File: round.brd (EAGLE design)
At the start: 50 x 50 mm, 8 parts, among them IC1 MC9S08GT8A-48, U1 USD-SOCKETNEW, U2 MCP73831, U3 ADXL345, U5 RFM69CW

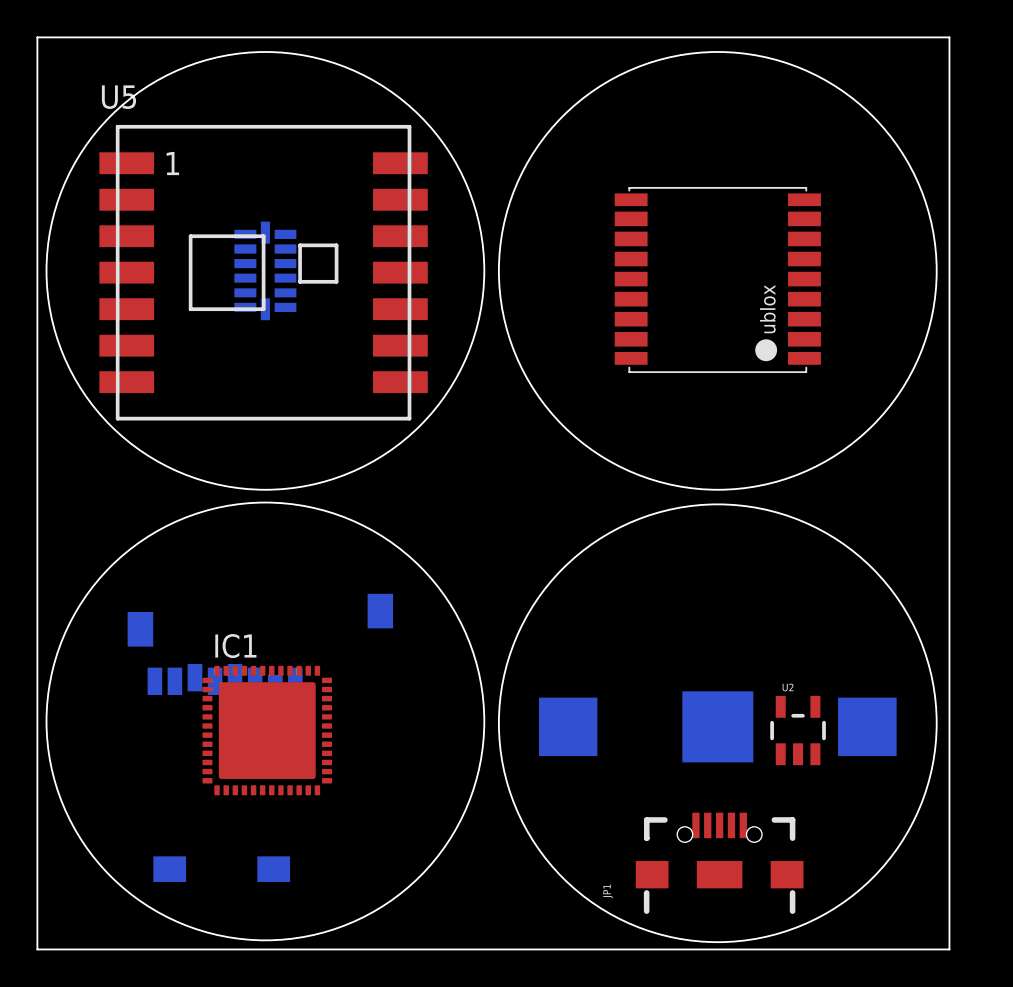
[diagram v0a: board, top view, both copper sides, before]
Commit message: Added power supply to round boards.
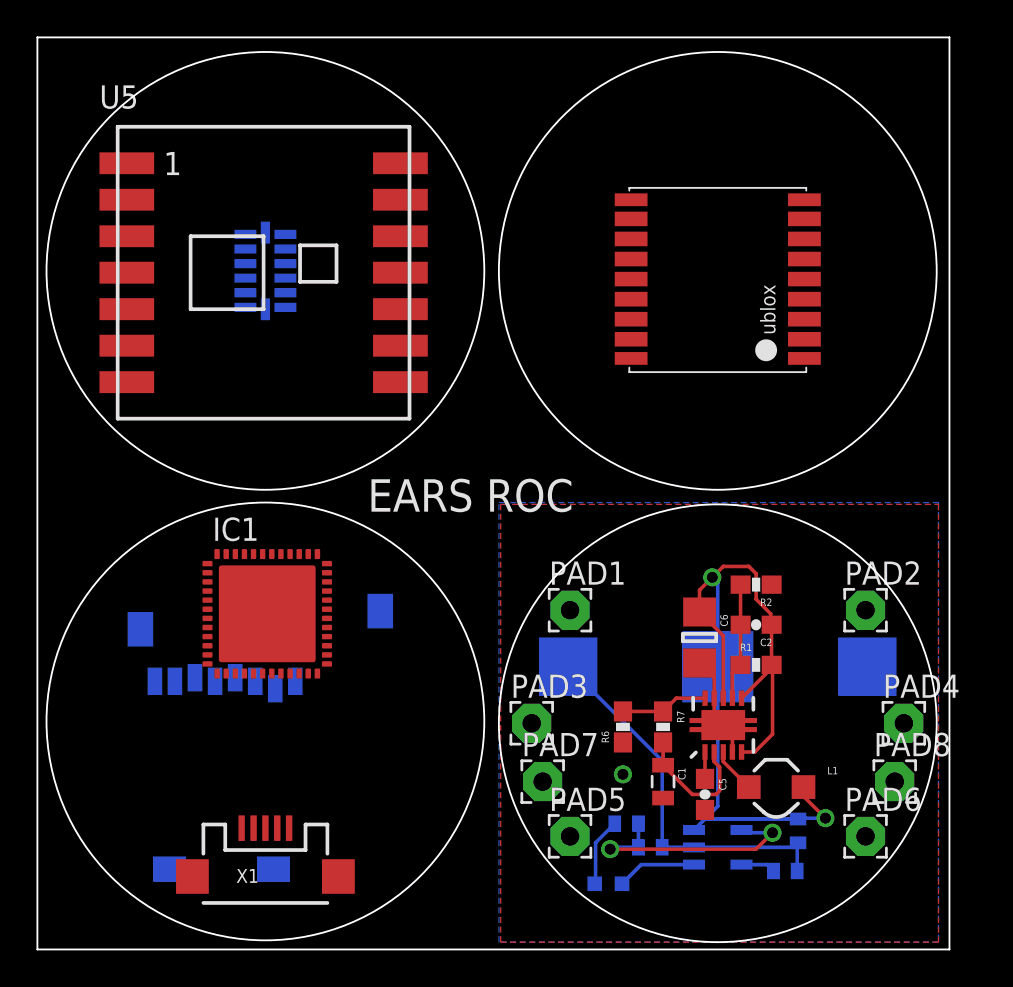
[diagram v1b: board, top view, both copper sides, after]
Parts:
- removed JP1: USB_MICROB_PLUGCONN-11752, SparkFun-Connectors:USB-B-MICRO-SMD_V03
- removed U2: MCP73831, SparkFun-PowerIC:SOT23-5
- added C1: 22uF, CH_passive:0805
- added C2, C5: 0.1uF, SparkFun:0603-CAP
- added C3, C4: 4.7uF, SparkFun:0402-CAP
- added C6: 10uF, CH_passive:1206
- added D11: RED, SparkFun:LED-0603
- added L1: 4.7uH, 1.2A, SparkFun:CDRH2D09
- added PAD1, PAD2, PAD3, PAD4, PAD5, PAD6, PAD7, PAD8: (no value), wirepad:2,15/1,0
- added R1, R7: 2M, SparkFun:0603-RES
- added R2, R6: 220k, SparkFun:0603-RES
- added R3: 330, SparkFun:0402-RES
- added R4: 2K, SparkFun:0402-RES
- added U4: MCP73831, SparkFun:SOT23-5
- added U6: TPS61200, SparkFun:QFN-10_PAD
- added X1: Micro USB, SparkFun:USB-MICROB
- moved IC1 6.40 mm to (12.6, 18.4)
- moved U$1 3.30 mm to (37.3, 15.5)
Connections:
- new net FB: R6.2, R7.1, U6.10
- new net N$1: C5.1, U6.1
- new net N$2: L1.P$1, U6.3
- new net N$3: D11.A, R3.1
- new net PROG: R4.1, U4.5
- new net STAT: D11.C, U4.1
- new net UVLO: C2.2, R1.1, R2.2, U6.7
- new net VCC: C1.1, R7.2, U6.2
- net GND: now also C1.2, C3.2, C4.2, C5.2, C6.2, R2.1, R4.2, R6.1, U$1.+$2, U4.2, U6.11, U6.12, U6.13, U6.14, U6.15, U6.4, U6.9, X1.GND
- net VBAT: now also C2.1, C4.1, C6.1, L1.P$2, R1.2, U$1.-, U4.3, U6.5, U6.6, U6.8; no longer U2.3
- net VIN: now also C3.1, R3.2, U4.4, X1.VBUS; no longer U2.4
- net VSS: no longer U2.2
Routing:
- net VBAT: track 0.00 -> 47.4 mm, vias 0 -> 2
- net GND: track 0.00 -> 30.0 mm, vias 0 -> 1
- net VIN: track 0.00 -> 13.9 mm, vias 0 -> 2
- net VCC: track 0.00 -> 7.34 mm
- net UVLO: track 0.00 -> 6.41 mm
- net FB: track 0.00 -> 4.80 mm
- net STAT: track 0.00 -> 4.38 mm
- net N$3: track 0.00 -> 3.76 mm
- net N$2: track 0.00 -> 2.50 mm
- net PROG: track 0.00 -> 1.89 mm
- net N$1: track 0.00 -> 1.47 mm
- added copper zone on layer 1, net GND
- added copper zone on layer 16, net GND
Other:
- board text added: "EARS ROC"
